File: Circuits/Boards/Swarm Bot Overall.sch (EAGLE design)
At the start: 17 parts, among them IC1 MEGA164P/324P/644P-AU, IC2 MCP73831

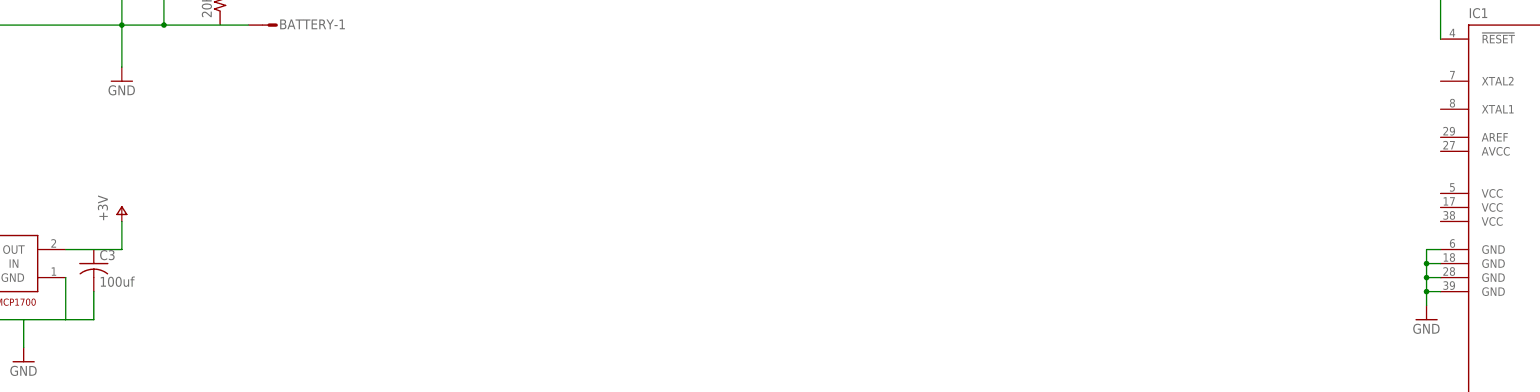
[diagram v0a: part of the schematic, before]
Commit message: 
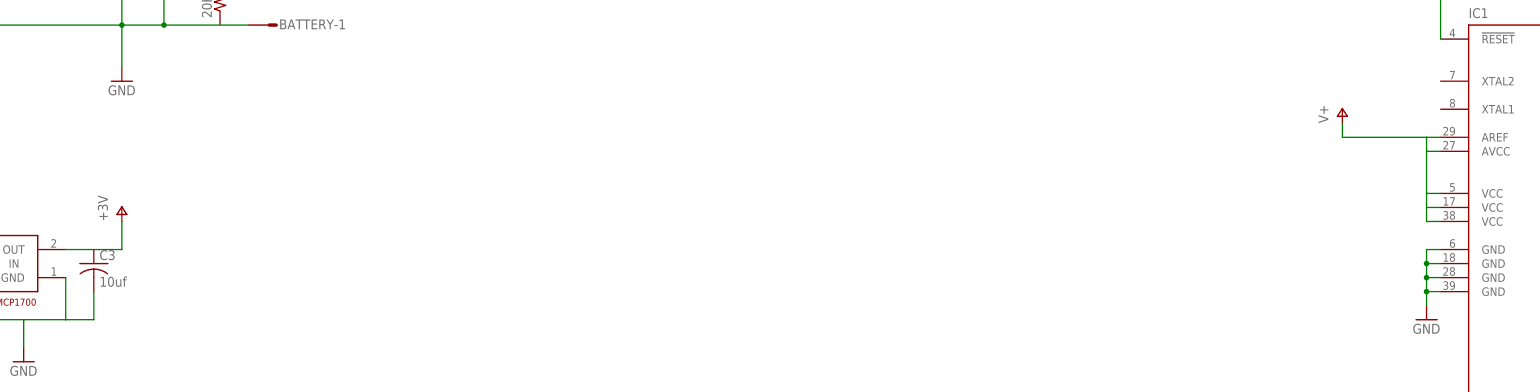
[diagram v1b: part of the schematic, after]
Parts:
- C3: value 100uf -> 10uf
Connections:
- net V+: now also IC1.AREF, IC1.AVCC, IC1.VCC@1, IC1.VCC@2, IC1.VCC@3
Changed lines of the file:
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@@
 <grid distance="0.1" unitdist="inch" unit="inch" style="lines" multiple="1" display="no" altdistance="0.01" altunitdist="inch" altunit="inch"/>
 <layers>
-<layer number="1" name="Top" color="4" fill="1" visible="yes" active="no"/>
-<layer number="16" name="Bottom" color="1" fill="1" visible="yes" active="no"/>
-<layer number="17" name="Pads" color="2" fill="1" visible="yes" active="no"/>
-<layer number="18" name="Vias" color="2" fill="1" visible="yes" active="no"/>
-<layer number="19" name="Unrouted" color="6" fill="1" visible="yes" active="no"/>
-<layer number="20" name="Dimension" color="15" fill="1" visible="yes" active="no"/>
-<layer number="21" name="tPlace" color="7" fill="1" visible="yes" active="no"/>
-<layer number="22" name="bPlace" color="7" fill="1" visible="yes" active="no"/>
-<layer number="23" name="tOrigins" color="15" fill="1" visible="yes" active="no"/>
-<layer number="24" name="bOrigins" color="15" fill="1" visible="yes" active="no"/>
-<layer number="25" name="tNames" color="7" fill="1" visible="yes" active="no"/>
-<layer number="26" name="bNames" color="7" fill="1" visible="yes" active="no"/>
-<layer number="27" name="tValues" color="7" fill="1" visible="yes" active="no"/>
-<layer number="28" name="bValues" color="7" fill="1" visible="yes" active="no"/>
+<layer number="1" name="Top" color="4" fill="1" visible="no" active="no"/>
+<layer number="16" name="Bottom" color="1" fill="1" visible="no" active="no"/>
+<layer number="17" name="Pads" color="2" fill="1" visible="no" active="no"/>
+<layer number="18" name="Vias" color="2" fill="1" visible="no" active="no"/>
+<layer number="19" name="Unrouted" color="6" fill="1" visible="no" active="no"/>
+<layer number="20" name="Dimension" color="15" fill="1" visible="no" active="no"/>
+<layer number="21" name="tPlace" color="7" fill="1" visible="no" active="no"/>
+<layer number="22" name="bPlace" color="7" fill="1" visible="no" active="no"/>
+<layer number="23" name="tOrigins" color="15" fill="1" visible="no" active="no"/>
+<layer number="24" name="bOrigins" color="15" fill="1" visible="no" active="no"/>
+<layer number="25" name="tNames" color="7" fill="1" visible="no" active="no"/>
+<layer number="26" name="bNames" color="7" fill="1" visible="no" active="no"/>
+<layer number="27" name="tValues" color="7" fill="1" visible="no" active="no"/>
+<layer number="28" name="bValues" color="7" fill="1" visible="no" active="no"/>
 <layer number="29" name="tStop" color="7" fill="3" visible="no" active="no"/>
 <layer number="30" name="bStop" color="7" fill="6" visible="no" active="no"/>
@@
 <layer number="35" name="tGlue" color="7" fill="4" visible="no" active="no"/>
 <layer number="36" name="bGlue" color="7" fill="5" visible="no" active="no"/>
-<layer number="37" name="tTest" color="7" fill="1" visible="yes" active="no"/>
-<layer number="38" name="bTest" color="7" fill="1" visible="yes" active="no"/>
+<layer number="37" name="tTest" color="7" fill="1" visible="no" active="no"/>
+<layer number="38" name="bTest" color="7" fill="1" visible="no" active="no"/>
 <layer number="39" name="tKeepout" color="4" fill="11" visible="no" active="no"/>
 <layer number="40" name="bKeepout" color="1" fill="11" visible="no" active="no"/>
@@
 <layer number="44" name="Drills" color="7" fill="1" visible="no" active="no"/>
 <layer number="45" name="Holes" color="7" fill="1" visible="no" active="no"/>
-<layer number="46" name="Milling" color="3" fill="1" visible="yes" active="no"/>
-<layer number="47" name="Measures" color="7" fill="1" visible="yes" active="no"/>
-<layer number="48" name="Document" color="7" fill="1" visible="yes" active="no"/>
-<layer number="49" name="Reference" color="7" fill="1" visible="yes" active="no"/>
-<layer number="50" name="dxf" color="7" fill="1" visible="yes" active="no"/>
-<layer number="51" name="tDocu" color="6" fill="1" visible="yes" active="no"/>
-<layer number="52" name="bDocu" color="7" fill="1" visible="yes" active="no"/>
+<layer number="46" name="Milling" color="3" fill="1" visible="no" active="no"/>
+<layer number="47" name="Measures" color="7" fill="1" visible="no" active="no"/>
+<layer number="48" name="Document" color="7" fill="1" visible="no" active="no"/>
+<layer number="49" name="Reference" color="7" fill="1" visible="no" active="no"/>
+<layer number="50" name="dxf" color="7" fill="1" visible="no" active="no"/>
+<layer number="51" name="tDocu" color="6" fill="1" visible="no" active="no"/>
+<layer number="52" name="bDocu" color="7" fill="1" visible="no" active="no"/>
 <layer number="91" name="Nets" color="2" fill="1" visible="yes" active="yes"/>
 <layer number="92" name="Busses" color="1" fill="1" visible="yes" active="yes"/>
@@
 <part name="GND4" library="supply1" deviceset="GND" device=""/>
 <part name="U$1" library="SwarmParts" deviceset="MCP1700T-3002E/TT" device=""/>
-<part name="C3" library="resistor" deviceset="C-US" device="025-050X050" value="100uf"/>
+<part name="C3" library="resistor" deviceset="C-US" device="025-050X050" value="10uf"/>
 <part name="C4" library="resistor" deviceset="C-US" device="025-050X050" value="10uf"/>
 <part name="P+3" library="supply1" deviceset="V+" device=""/>
 <part name="GND5" library="supply1" deviceset="GND" device=""/>
 <part name="P+4" library="supply1" deviceset="V+" device="" value="+3V"/>
+<part name="P+5" library="supply1" deviceset="V+" device=""/>
 </parts>
 <sheets>
@@
 <instance part="GND5" gate="1" x="-101.6" y="88.9"/>
 <instance part="P+4" gate="1" x="-83.82" y="116.84"/>
+<instance part="P+5" gate="1" x="137.16" y="134.62"/>
 </instances>
 <busses>
@@
 <pinref part="P+3" gate="1" pin="V+"/>
 </segment>
-</net>
+<segment>
+<pinref part="IC1" gate="G$1" pin="VCC@3"/>
+<wire x1="154.94" y1="114.3" x2="152.4" y2="114.3" width="0.1524" layer="91"/>
+<wire x1="152.4" y1="114.3" x2="152.4" y2="116.84" width="0.1524" layer="91"/>
+<wire x1="152.4" y1="116.84" x2="152.4" y2="119.38" width="0.1524" layer="91"/>
+<wire x1="152.4" y1="119.38" x2="152.4" y2="127" width="0.1524" layer="91"/>
+<wire x1="152.4" y1="127" x2="152.4" y2="129.54" width="0.1524" layer="91"/>
+<wire x1="152.4" y1="129.54" x2="137.16" y2="129.54" width="0.1524" layer="91"/>
+<pinref part="P+5" gate="1" pin="V+"/>
+<wire x1="137.16" y1="129.54" x2="137.16" y2="132.08" width="0.1524" layer="91"/>
+<pinref part="IC1" gate="G$1" pin="AREF"/>
+<wire x1="154.94" y1="129.54" x2="152.4" y2="129.54" width="0.1524" layer="91"/>
+<pinref part="IC1" gate="G$1" pin="AVCC"/>
+<wire x1="154.94" y1="127" x2="152.4" y2="127" width="0.1524" layer="91"/>
+<pinref part="IC1" gate="G$1" pin="VCC@1"/>
+<wire x1="154.94" y1="119.38" x2="152.4" y2="119.38" width="0.1524" layer="91"/>
+<pinref part="IC1" gate="G$1" pin="VCC@2"/>
+<wire x1="154.94" y1="116.84" x2="152.4" y2="116.84" width="0.1524" layer="91"/>
+</segment>
+</net>

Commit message: massive eagle update
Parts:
- removed 10K, 20K: (no value), resistor:R-US_0204/5
- removed BATTERY: (no value), con-amp-quick:M02S
- removed IC1: MEGA164P/324P/644P-AU, avr-5:MEGA164P/324P/644P-AU
- removed IC2: MCP73831, microchip-update-2:MCP73831
- removed SL1: (no value), con-amp-quick:M05
- removed SL2: (no value), con-amp-quick:M03
- removed U$1: MCP1700T-3002E/TT, SwarmParts:MCP1700T-3002E/TT
- added B1: PIEZOBUZZER, Passive:PIEZOBUZZER
- added C5: 4.7uf, Passive:CAP0603
- added CON1: ISP(2X3), Mechanical:ISP(2X3)
- added CON2: FTDI, Mechanical:FTDI
- added LED1: LED, Passive:LED
- added PR1: 500k-20k, Passive:CDSPHOTORESISTOR
- added R6: 15k, Passive:RES0603
- added R7: 10k, Passive:RES0603
- added R8: 1k, Passive:RES0603
- added R9: 20k, Passive:RES0603
- added T1: NPN, Passive:NPN
- added U1: ATMEGA324P, DigitalIC:ATMEGA324P
- added U2: MCP73832SOT-23, PowerIC:MCP73832SOT-23
- added V1: MCP1700-3002E, PowerIC:MCP1700-3002E
- C1: value 4.7uf -> 1uf; device resistor:C-US025-050X050 -> Passive:CAP0603
- C2: value 4.7uf -> 10uf; device resistor:C-US050-025X075 -> Passive:CAP0805
- C3: value 10uf -> 1uf; device resistor:C-US025-050X050 -> Passive:CAP0603
- C4: value 10uf -> 4.7uf; device resistor:C-US025-050X050 -> Passive:CAP0603
- R1: device resistor:R-US_0204/5 -> Passive:RES0603
- R2: value 20k -> 1.5k; device resistor:R-US_0204/5 -> Passive:RES0603
- R3: value 20k -> 400; device resistor:R-US_0204/5 -> Passive:RES0603
- R4: value 20k -> 600; device resistor:R-US_0204/5 -> Passive:RES0603
- R5: value 20k -> 10k; device resistor:R-US_0204/5 -> Passive:RES0603
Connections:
- removed net +5V: C1.1, IC2.VDD, R2.2
- removed net 3V: U$1.OUT
- removed net CHARGESTATE: R4.1, R5.2
- removed net V+: 10K.2, BATTERY-2.S, C2.1, IC1.AREF, IC1.AVCC, IC1.VCC@1, IC1.VCC@2, IC1.VCC@3, IC2.VBAT, U$1.IN
- removed net VOLTAGEDETECT: R2.1, R3.2
- new net +3V: B1.+, C2.1, C3.1, PR1.2, R7.1, R8.2, U1.AREF, U1.AVCC, U1.VCC, V1.OUT
- new net +VBAT: C1.1, C4.1, R5.2, U2.VBAT, V1.IN
- new net +VCHG: C5.1, R2.2, R3.2, U2.VDD
- new net BUZZER: T1.B, U1.PD7(PCINT31/OC2A)
- new net CHGDETECT: R3.1, R4.2
- new net CHGSTATUS: LED1.C, U2.STAT
- new net LIGHTSENSE: PR1.1, R9.2, U1.PA1(ADC1/PCINT1)
- new net LINESENSE1: U1.PA2(ADC2/PCINT2)
- new net LINESENSE2: U1.PA3(ADC3/PCINT3)
- new net OBJECTSENSOR: U1.PA4(ADC4/PCINT4)
- new net VSENSE: R5.1, R6.2, U1.PA0(ADC0/PCINT0)
- net GND: now also C5.2, CON1.GND, CON2.GND, R1.1, R4.1, R6.1, R9.1, T1.E, U1.GND, U2.VSS, V1.GND; no longer BATTERY-1.S, IC1.GND@1, IC1.GND@2, IC1.GND@3, IC1.GND@4, IC2.VSS, R1.2, R3.1, R5.1, SL1.5, SL2.3, U$1.GND
- net N$1: now also R1.2, U2.PROG; no longer IC2.PROG, R1.1
- net N$2: now also CON1.MOSI, U1.PB5(PCINT13/MOSI); no longer IC1.(TXD0/PCINT25)PD1, SL2.2
- net N$3: now also CON1.MISO, U1.PB6(PCINT14/MISO); no longer 10K.1, 20K.2
- net N$4: now also LED1.A, R2.1; no longer IC1.(RXD0/PCINT24)PD0, SL2.1
- net N$5: now also CON1.SCK, U1.PB7(PCINT15/SCK); no longer IC1.(MOSI/PCINT13)PB5, SL1.2
- net N$6: now also CON1.!RESET, R7.2, U1.!RESET; no longer IC2.STAT, R4.2
- net N$7: now also CON2.RXI, U1.PD1(PCINT25/TXD0); no longer IC1.(MISO/PCINT14)PB6, SL1.3
- net N$8: now also CON2.TXO, U1.PD0(PCINT24/RXD0); no longer IC1.(SCK/PCINT15)PB7, SL1.4
- net N$9: now also B1.-, R8.1, T1.C; no longer IC1.!RESET, SL1.1
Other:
- note added: "4.6v ideal"
- moved on the sheet: C1, C2, C3, C4, R1, R2, R3, R4, R5

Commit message: updates to swarm board circuit
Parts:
- added C6, C7: 10uf, Passive:CAP0805
- added LED13, LED2, LED3, LED4, LED5, LED6, LED7: IR, Passive:LED5MMRA
- added R10, R11, R12, R13, R14, R15, R17, R18, R19, R20, R21, R22, R24: (no value), Passive:RES0603
- added R16, R23: 500, Passive:RES0603
- added T2, T3: NPN2N2222, Passive:NPN2N2222
- added T4, T5, T6, T7, T8, T9: TEFT4300, Passive:TEFT4300
- LED1: value LED -> (none); device Passive:LED -> Passive:LED0603
- T1: value NPN -> NPN2N2222; device Passive:NPN -> Passive:NPN2N2222
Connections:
- removed net OBJECTSENSOR: U1.PA4(ADC4/PCINT4)
- new net DISTANCELED: R23.1
- new net N$10: R10.1, R11.1, R12.1, R13.1, R14.1, R15.1, T2.C
- new net N$11: R16.2, T2.B
- new net N$12: R22.1, T3.C
- new net N$13: LED2.C, R10.2
- new net N$14: LED3.C, R11.2
- new net N$15: LED4.C, R12.2
- new net N$16: LED5.C, R13.2
- new net N$17: LED6.C, R14.2
- new net N$18: LED7.C, R15.2
- new net N$19: R23.2, T3.B
- new net N$25: LED13.C, R22.2
- new net R_A: R17.2, T4.E
- new net R_D: R18.2, R19.2, R20.2, R21.2, R24.2, T5.E, T6.E, T7.E, T8.E, T9.E
- new net TRANSMITLEDS: R16.1
- net +3V: now also C6.1, C7.1, LED13.A, LED2.A, LED3.A, LED4.A, LED5.A, LED6.A, LED7.A, T4.C, T5.C, T6.C, T7.C, T8.C, T9.C
- net GND: now also C6.2, C7.2, R17.1, R18.1, R19.1, R20.1, R21.1, R24.1, T2.E, T3.E
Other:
- moved on the sheet: B1, C1, C2, C4, C5, LED1, PR1, R1, R2, R3, R4, R5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

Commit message: more work
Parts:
- added C8, C9: 1uf, Passive:CAP0603
- added LED10, LED8, LED9: (no value), Passive:LED0603
- added R25, R26, R27, R28: (no value), Passive:RES0603
- added U3: TB6552FN/FNG, DigitalIC:TB6552FN/FNG
- CON2: value FTDI -> FTDI(1X6); device Mechanical:FTDI -> Mechanical:FTDI(1X6)
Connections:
- new net AIN1: U3.AIN1
- new net AIN2: U3.AIN2
- new net APWM: U3.APWM
- new net BIN1: U3.BIN1
- new net BIN2: U3.BIN2
- new net BPWM: U3.BPWM
- new net LED1: R25.1
- new net LED2: R26.1
- new net LED3: R27.1
- new net MA+: U3.AO1
- new net MA-: U3.AO2
- new net MB+: U3.BO1
- new net MB-: U3.BO2
- new net N$20: LED8.C, R25.2
- new net N$21: LED9.C, R26.2
- new net N$22: LED10.C, R27.2
- new net N$23: C9.2
- new net N$24: LED10.A, LED8.A
- new net N$26: R28.2, T1.B
- new net STBY: U3.ASTBY, U3.BSTBY
- net +3V: now also C8.1, LED9.A, U3.VCC
- net +VBAT: now also C9.1, U3.VM
- net BUZZER: now also R28.1; no longer T1.B, U1.PD7(PCINT31/OC2A)
- net GND: now also C8.2, U3.GND, U3.PGND
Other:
- moved on the sheet: CON2
